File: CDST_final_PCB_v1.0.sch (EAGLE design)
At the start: 94 parts, among them IC1 MIC_I2S_SPH0645, IC2 LM2596S, IC3 CP2101, P1 ZX62D-B-5P8, Q1 BCX70SMD, Q2 BCX70SMD, U1 AD8232ACPZ-R7, U3 ESP-WROOM-03

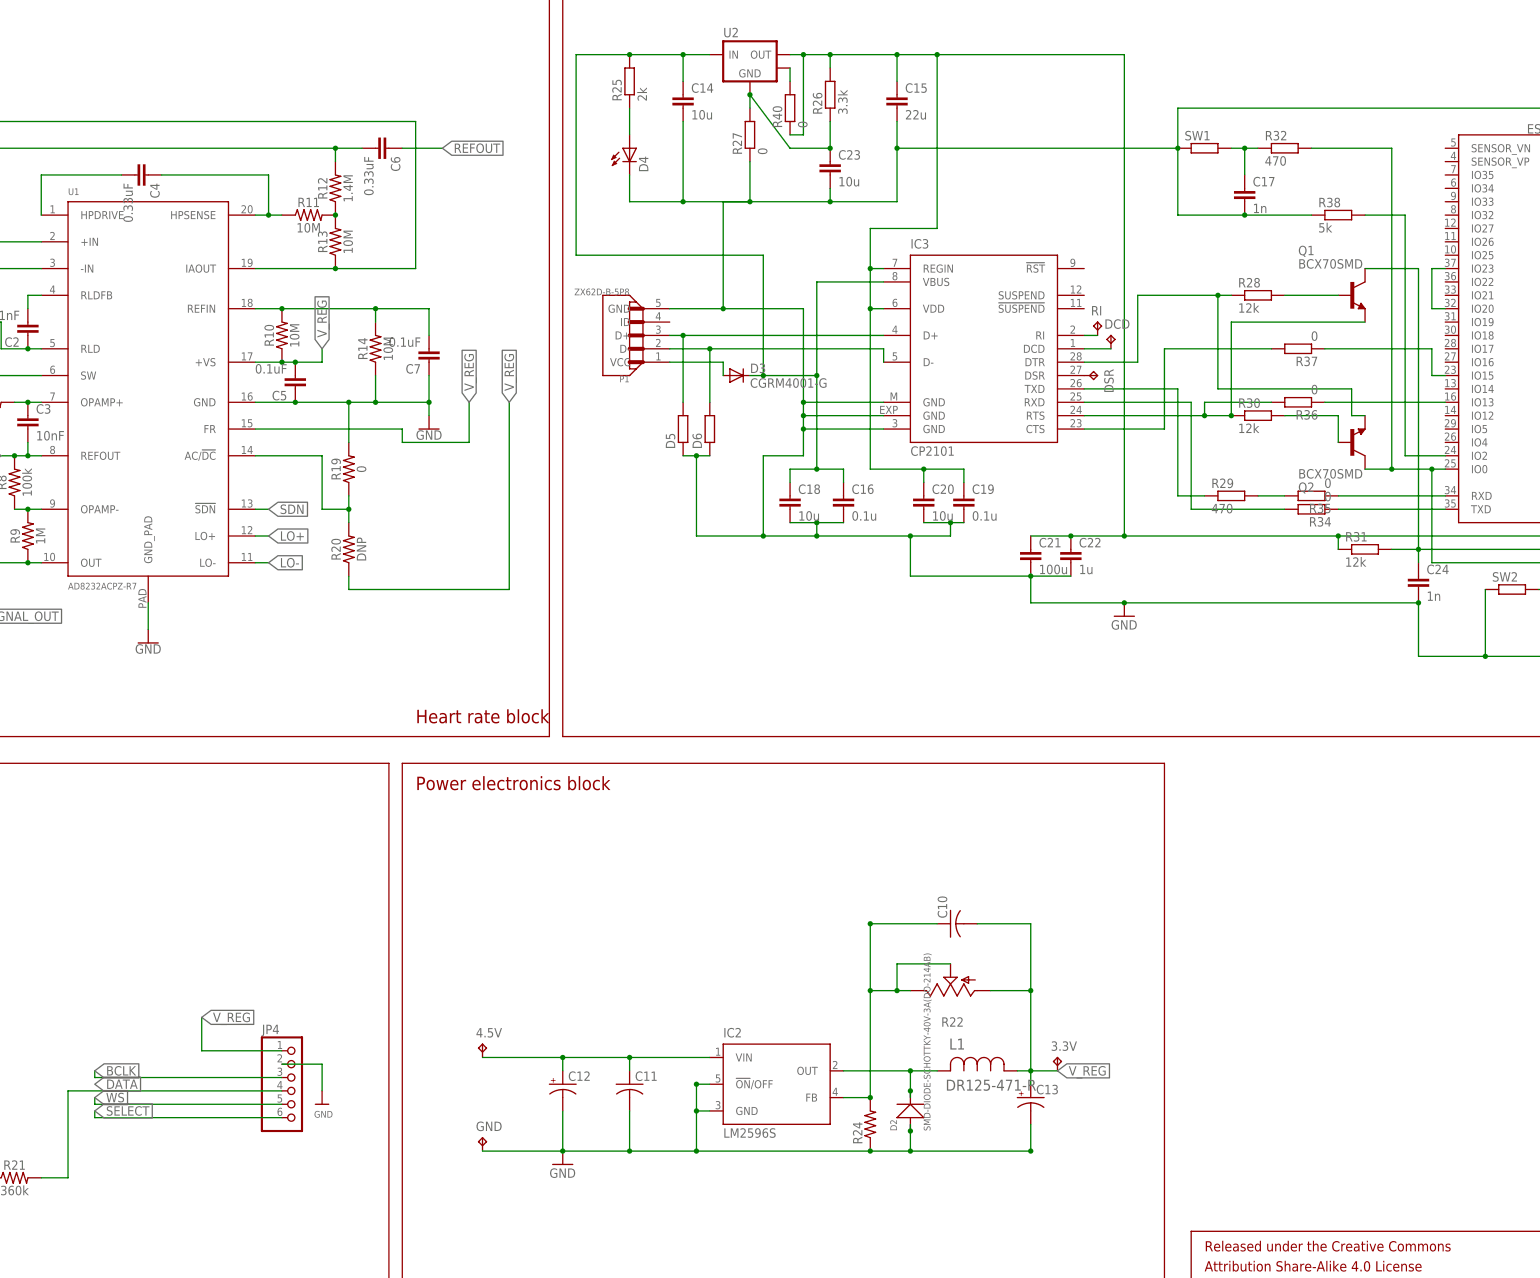
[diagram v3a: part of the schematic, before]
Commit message: Test pin added to ESP
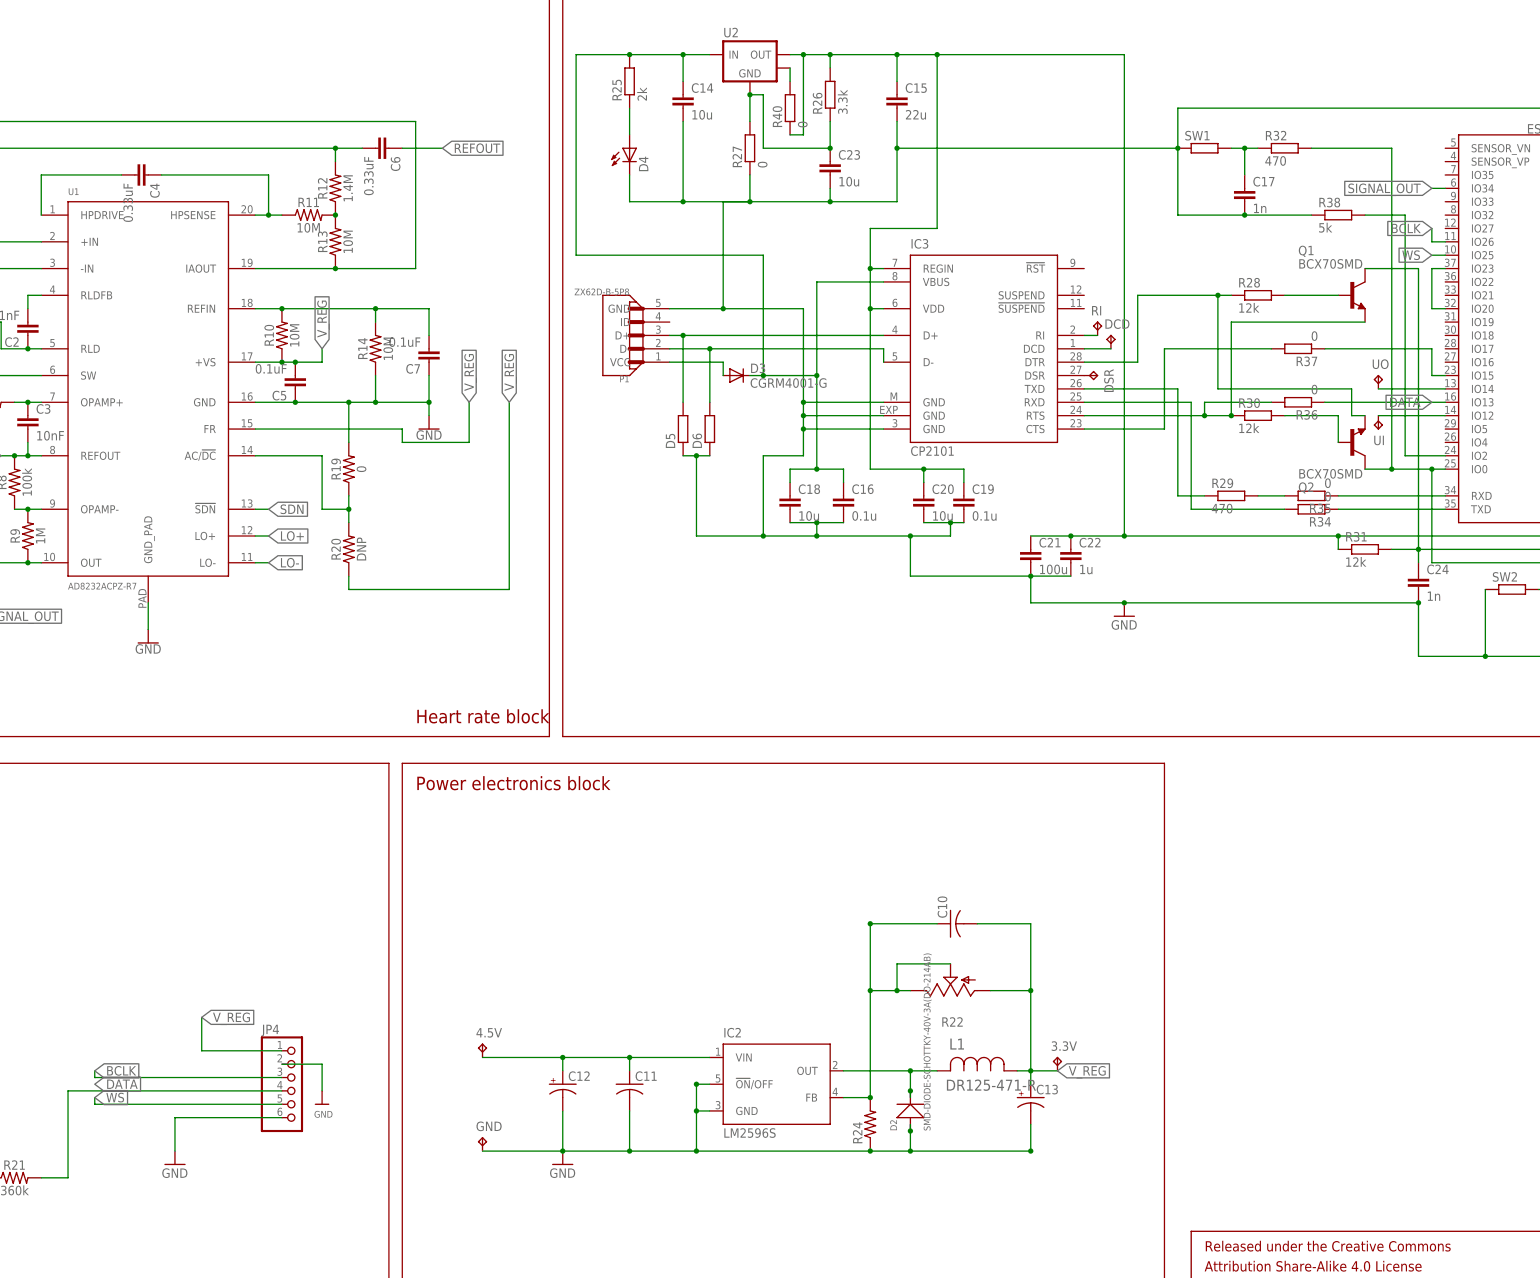
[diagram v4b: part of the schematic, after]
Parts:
- added UI, UO: TPB1,27, testpad:TPB1,27
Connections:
- new net N$32: U3.IO14, UO.TP
- net BCLK: now also U3.IO26
- net DATA: now also R36.1, U3.IO13
- net GND: now also JP4.6
- net N$41: now also U3.IO12, UI.TP; no longer R36.1, U3.IO13
- net SELECT: no longer JP4.6
- net SIGNAL_OUT: now also U3.IO34
- net WS: now also U3.IO25
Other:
- moved on the sheet: R27
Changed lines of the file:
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@@
 <?xml version="1.0" encoding="utf-8"?>
 <!DOCTYPE eagle SYSTEM "eagle.dtd">
-<eagle version="8.4.1">
+<eagle version="8.3.2">
 <drawing>
 <settings>
@@
 <layer number="18" name="Vias" color="2" fill="1" visible="no" active="no"/>
 <layer number="19" name="Unrouted" color="6" fill="1" visible="no" active="no"/>
-<layer number="20" name="Dimension" color="15" fill="1" visible="no" active="no"/>
-<layer number="21" name="tPlace" color="16" fill="1" visible="no" active="no"/>
+<layer number="20" name="Dimension" color="24" fill="1" visible="no" active="no"/>
+<layer number="21" name="tPlace" color="7" fill="1" visible="no" active="no"/>
 <layer number="22" name="bPlace" color="7" fill="1" visible="no" active="no"/>
 <layer number="23" name="tOrigins" color="15" fill="1" visible="no" active="no"/>
@@
 <layer number="49" name="Reference" color="7" fill="1" visible="no" active="no"/>
 <layer number="50" name="dxf" color="7" fill="1" visible="no" active="no"/>
-<layer number="51" name="tDocu" color="14" fill="1" visible="no" active="no"/>
+<layer number="51" name="tDocu" color="7" fill="1" visible="no" active="no"/>
 <layer number="52" name="bDocu" color="7" fill="1" visible="no" active="no"/>
 <layer number="53" name="tGND_GNDA" color="7" fill="9" visible="no" active="no"/>
@@
 <part name="DSR" library="testpad" library_urn="urn:adsk.eagle:library:385" deviceset="TP" device="B2,54" package3d_urn="urn:adsk.eagle:package:27948/1"/>
 <part name="RI" library="testpad" library_urn="urn:adsk.eagle:library:385" deviceset="TP" device="B2,54" package3d_urn="urn:adsk.eagle:package:27948/1"/>
+<part name="GND7" library="supply1" library_urn="urn:adsk.eagle:library:371" deviceset="GND" device=""/>
+<part name="UI" library="testpad" library_urn="urn:adsk.eagle:library:385" deviceset="TP" device="B1,27" package3d_urn="urn:adsk.eagle:package:27944/1"/>
+<part name="UO" library="testpad" library_urn="urn:adsk.eagle:library:385" deviceset="TP" device="B1,27" package3d_urn="urn:adsk.eagle:package:27944/1"/>
 </parts>
 <sheets>
@@
 <instance part="R25" gate="G$1" x="17.78" y="127" rot="R90"/>
 <instance part="R26" gate="G$1" x="55.88" y="124.46" rot="R90"/>
-<instance part="R27" gate="G$1" x="40.64" y="116.84" rot="R90"/>
+<instance part="R27" gate="G$1" x="40.64" y="114.3" rot="R90"/>
 <instance part="R28" gate="G$1" x="137.16" y="86.36"/>
 <instance part="R29" gate="G$1" x="132.08" y="48.26"/>
@@
 <instance part="DSR" gate="G$1" x="106.68" y="71.12" rot="R270"/>
 <instance part="RI" gate="G$1" x="106.68" y="81.28"/>
+<instance part="GND7" gate="1" x="-68.58" y="-78.74"/>
+<instance part="UI" gate="G$1" x="160.02" y="60.96" rot="R180"/>
+<instance part="UO" gate="G$1" x="160.02" y="71.12"/>
 </instances>
 <busses>
@@
 <pinref part="U2" gate="U1" pin="GND"/>
 <pinref part="R27" gate="G$1" pin="2"/>
-<wire x1="40.64" y1="121.92" x2="40.64" y2="124.46" width="0.1524" layer="91"/>
-<wire x1="40.64" y1="124.46" x2="48.26" y2="114.3" width="0.1524" layer="91"/>
+<wire x1="40.64" y1="119.38" x2="40.64" y2="124.46" width="0.1524" layer="91"/>
+<wire x1="40.64" y1="124.46" x2="43.18" y2="124.46" width="0.1524" layer="91"/>
+<wire x1="43.18" y1="124.46" x2="43.18" y2="114.3" width="0.1524" layer="91"/>
 <junction x="40.64" y="124.46"/>
 <pinref part="R26" gate="G$1" pin="1"/>
 <wire x1="55.88" y1="119.38" x2="55.88" y2="114.3" width="0.1524" layer="91"/>
-<wire x1="48.26" y1="114.3" x2="55.88" y2="114.3" width="0.1524" layer="91"/>
+<wire x1="43.18" y1="114.3" x2="55.88" y2="114.3" width="0.1524" layer="91"/>
 <pinref part="C23" gate="G$1" pin="1"/>
 <junction x="55.88" y="114.3"/>
@@
 <wire x1="17.78" y1="104.14" x2="17.78" y2="109.22" width="0.1524" layer="91"/>
 <pinref part="R27" gate="G$1" pin="1"/>
-<wire x1="40.64" y1="111.76" x2="40.64" y2="104.14" width="0.1524" layer="91"/>
+<wire x1="40.64" y1="109.22" x2="40.64" y2="104.14" width="0.1524" layer="91"/>
 <wire x1="40.64" y1="104.14" x2="27.94" y2="104.14" width="0.1524" layer="91"/>
 <junction x="27.94" y="104.14"/>
@@
 <pinref part="D6" gate="G$1" pin="1"/>
 </segment>
+<segment>
+<pinref part="GND7" gate="1" pin="GND"/>
+<wire x1="-68.58" y1="-76.2" x2="-68.58" y2="-69.85" width="0.1524" layer="91"/>
+<pinref part="JP4" gate="A" pin="6"/>
+<wire x1="-48.26" y1="-69.85" x2="-68.58" y2="-69.85" width="0.1524" layer="91"/>
+</segment>
 </net>
 <net name="SIGNAL_OUT" class="0">
@@
 <label x="-147.32" y="35.56" size="1.778" layer="95" xref="yes"/>
 </segment>
+<segment>
+<pinref part="U3" gate="G$1" pin="IO34"/>
+<wire x1="172.72" y1="106.68" x2="170.18" y2="106.68" width="0.1524" layer="91"/>
+<label x="170.18" y="106.68" size="1.778" layer="95" rot="R180" xref="yes"/>
+</segment>
 </net>
 <net name="LA" class="0">
@@
 <label x="-83.82" y="-66.04" size="1.778" layer="95" xref="yes"/>
 </segment>
+<segment>
+<pinref part="U3" gate="G$1" pin="IO25"/>
+<wire x1="172.72" y1="93.98" x2="170.18" y2="93.98" width="0.1524" layer="91"/>
+<label x="170.18" y="93.98" size="1.778" layer="95" rot="R180" xref="yes"/>
+</segment>
 </net>
 <net name="SELECT" class="0">
@@
 <wire x1="-175.26" y1="-81.28" x2="-175.26" y2="-88.9" width="0.1524" layer="91"/>
 </segment>
-<segment>
-<pinref part="JP4" gate="A" pin="6"/>
-<wire x1="-48.26" y1="-69.85" x2="-83.82" y2="-69.85" width="0.1524" layer="91"/>
-<wire x1="-83.82" y1="-69.85" x2="-83.82" y2="-68.58" width="0.1524" layer="91"/>
-<label x="-83.82" y="-68.58" size="1.778" layer="95" xref="yes"/>
-</segment>
 </net>
 <net name="BCLK" class="0">
@@
 <wire x1="-83.82" y1="-62.23" x2="-83.82" y2="-60.96" width="0.1524" layer="91"/>
 <label x="-83.82" y="-60.96" size="1.778" layer="95" xref="yes"/>
+</segment>
+<segment>
+<pinref part="U3" gate="G$1" pin="IO26"/>
+<wire x1="172.72" y1="96.52" x2="170.18" y2="96.52" width="0.1524" layer="91"/>
+<wire x1="170.18" y1="96.52" x2="170.18" y2="99.06" width="0.1524" layer="91"/>
+<label x="170.18" y="99.06" size="1.778" layer="95" rot="R180" xref="yes"/>
 </segment>
 </net>
@@
 <pinref part="R13" gate="G$1" pin="2"/>
 <junction x="-38.1" y="101.6"/>
-<pinref part="R13" gate="G$1" pin="2"/>
 </segment>
 </net>
@@
 <wire x1="-88.9" y1="-81.28" x2="-93.98" y2="-81.28" width="0.1524" layer="91"/>
 <label x="-83.82" y="-63.5" size="1.778" layer="95" xref="yes"/>
+</segment>
+<segment>
+<pinref part="R36" gate="G$1" pin="1"/>
+<pinref part="U3" gate="G$1" pin="IO13"/>
+<wire x1="149.86" y1="66.04" x2="172.72" y2="66.04" width="0.1524" layer="91"/>
+<label x="170.18" y="66.04" size="1.778" layer="95" rot="R180" xref="yes"/>
 </segment>
 </net>
@@
 </segment>
 </net>
-<net name="N$41" class="0">
-<segment>
-<pinref part="R36" gate="G$1" pin="1"/>
-<pinref part="U3" gate="G$1" pin="IO13"/>
-<wire x1="149.86" y1="66.04" x2="172.72" y2="66.04" width="0.1524" layer="91"/>
-</segment>
-</net>
 <net name="N$42" class="0">
 <segment>
@@
 </segment>
 </net>
+<net name="N$32" class="0">
+<segment>
+<pinref part="UO" gate="G$1" pin="TP"/>
+<pinref part="U3" gate="G$1" pin="IO14"/>
+<wire x1="160.02" y1="68.58" x2="172.72" y2="68.58" width="0.1524" layer="91"/>
+</segment>
+</net>
+<net name="N$41" class="0">
+<segment>
+<pinref part="UI" gate="G$1" pin="TP"/>
+<pinref part="U3" gate="G$1" pin="IO12"/>
+<wire x1="160.02" y1="63.5" x2="172.72" y2="63.5" width="0.1524" layer="91"/>
+</segment>
+</net>

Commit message: layout revision v0.1
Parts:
- added D7: RED, SparkFun-LED:LED-RED1206
- added R41: 10k, SparkFun-Resistors:RESISTOR1206
- added S1: (no value), SparkFun-Switches:SWITCH-SPDT-SMD-RIGHT-ANGLE
- added U4: 74LVC1G08SE, SparkFun-IC-Logic:74LVC08SE
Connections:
- new net N$47: D7.A, S1.O
- new net N$48: R21.2, U4G1.B
- new net N$49: R41.1, S1.P, U4G1.A
- net DATA: now also U4G1.Y; no longer R21.2
- net GND: now also D7.C, U4G2.P$V-
- net V_REG: now also R41.2, U4G2.P$V+
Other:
- moved on the sheet: C8, C9
